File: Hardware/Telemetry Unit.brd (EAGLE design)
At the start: 160 x 100 mm, 12 parts, among them IC1 MEGA128-A, Q1 10MHz, U1 MPL3115A2, X1 SMA-142-0701-801/806

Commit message: First Pass at Compact Layout
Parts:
- removed X1: SMA-142-0701-801/806, con-coax:J502-ND-142-0701-801/806
- added B1: 9V_CLIP, TrackerPeripherals:9V_CLIP
- added C10, C9: 22u, resistor:C0805
- added C11, C7, C8: 22p, resistor:C0603
- added C5, C6: 2.2u, resistor:C0603
- added D1: (no value), diode:DO214AC
- added FIX, PWR: (no value), led:SML0603
- added L1: 1.8n, TrackerPeripherals:L0603
- added L2: 6.8u, TrackerPeripherals:L1210
- added R1, R6: 10k, resistor:R0603
- added R10: 100k, resistor:R0603
- added R11, R2: 470, resistor:R0603
- added R3: 30k, resistor:R0603
- added R7: 40.2k, resistor:R0603
- added R8: 59k, resistor:R0603
- added R9: 13k, resistor:R0603
- added S1: TACT_SW_4.5MM, TrackerPeripherals:TACT_SW_4.5MM
- added U2: AP65111A, TrackerPeripherals:TSOT23-6
- C1: value (none) -> 2.2u
- GPS1: value TESO-LIV3F -> M20048-1; device ITCPeripherals:TESEO-LIV3F -> TrackerPeripherals:M20048-1
- Q1: device crystal:CTS406 -> crystal:HC49UP
- U1: device ITCPeripherals:LGA8 -> TrackerPeripherals:LGA8
- moved C2 41.3 mm to (4.19, 32.4), turned to 180 degrees
- moved C1 35.4 mm to (4.19, 29.8), turned to 180 degrees
- moved C3 31.1 mm to (27.9, 32.4), turned to 180 degrees
- moved C4 30.3 mm to (20.3, 32.4)
- moved XB1 28.3 mm to (34.3, 47.6), turned to 0 degrees
- moved R4 26.6 mm to (13.6, 28.7), turned to 180 degrees
- moved R5 22.2 mm to (13.6, 26.5), turned to 180 degrees
- moved U1 22.2 mm to (7.62, 31.8)
- moved Q1 21.7 mm to (24.1, 27.9)
- moved GPS1 19.2 mm to (11.4, 54.6), turned to 0 degrees
- moved IC1 6.35 mm to (12.7, 15.2), turned to 180 degrees
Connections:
- net N$5 renamed XTAL1
- new net !GPS_SLP: GPS1.26, IC1.30
- new net !RST: IC1.20, R1.2, S1.P$3, XB1.17
- new net FIX: GPS1.18, IC1.29, R2.1
- new net N$10: R8.1, U2.6
- new net N$12: C11.1, U2.4
- new net N$14: PWR.A, R11.2
- new net N$3: C7.2, GPS1.6
- new net N$5: IC1.61, R3.2, R6.1
- new net N$6: FIX.A, R2.2
- new net N$7: C11.2, L2.1, U2.3
- new net N$8: R7.2, R8.2, R9.1
- new net N$9: R10.2, U2.5
- new net PROG_PWR: D1.A, XB1.11
- new net RF_SLP: IC1.31, XB1.9
- new net VBAT: B1.V+, C10.1, D1.C, R10.1, R3.1, U2.1
- new net XTAL2: C3.1, IC1.23, Q1.2
- net +3V3: now also C5.1, C6.1, C8.1, C9.1, GPS1.12, L2.2, R1.1, R11.1, R7.1; no longer GPS1.14, GPS1.6, GPS1.7
- net GND: now also B1.V-, C10.2, C5.2, C6.2, C8.2, C9.2, FIX.C, GPS1.15, GPS1.16, GPS1.17, GPS1.19, GPS1.2, GPS1.22, GPS1.23, GPS1.24, GPS1.25, GPS1.27, GPS1.3, GPS1.5, GPS1.7, GPS1.9, L1.2, PWR.C, R6.2, R9.2, S1.P$2, U2.2; no longer GPS1.1, GPS1.10, GPS1.12, X1.G@1, X1.G@2, X1.G@3, X1.G@4
- net N$1: now also C7.1, GPS1.4; no longer GPS1.11, X1.1
- net N$4: now also GPS1.28, L1.1; no longer C3.1, IC1.23, Q1.3
- net RX1: now also GPS1.20; no longer GPS1.2
- net TX1: now also GPS1.21; no longer GPS1.3
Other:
- board size 160 x 100 mm -> 63.5 x 63.5 mm

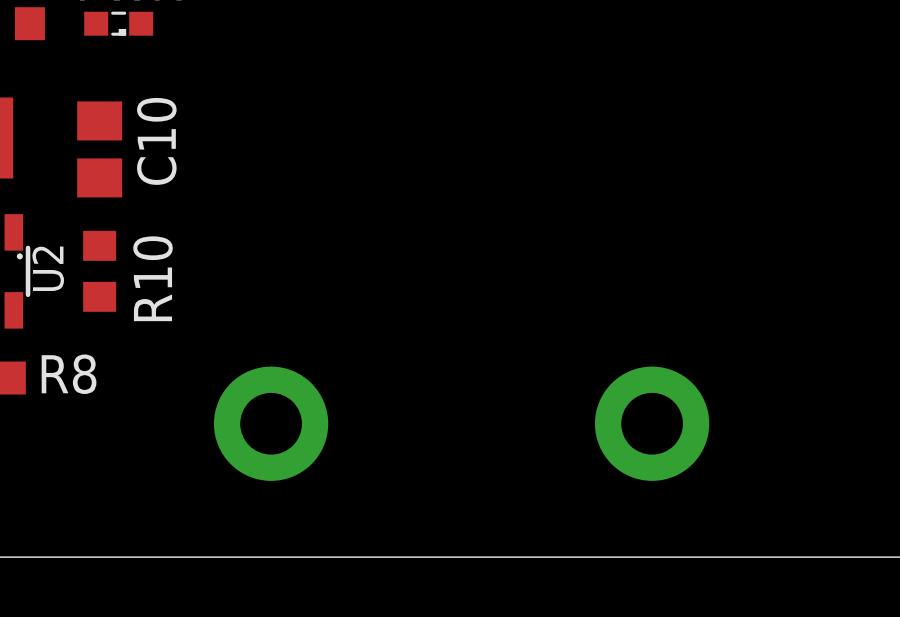
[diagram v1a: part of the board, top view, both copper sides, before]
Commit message: Switch to screw terminals for battery
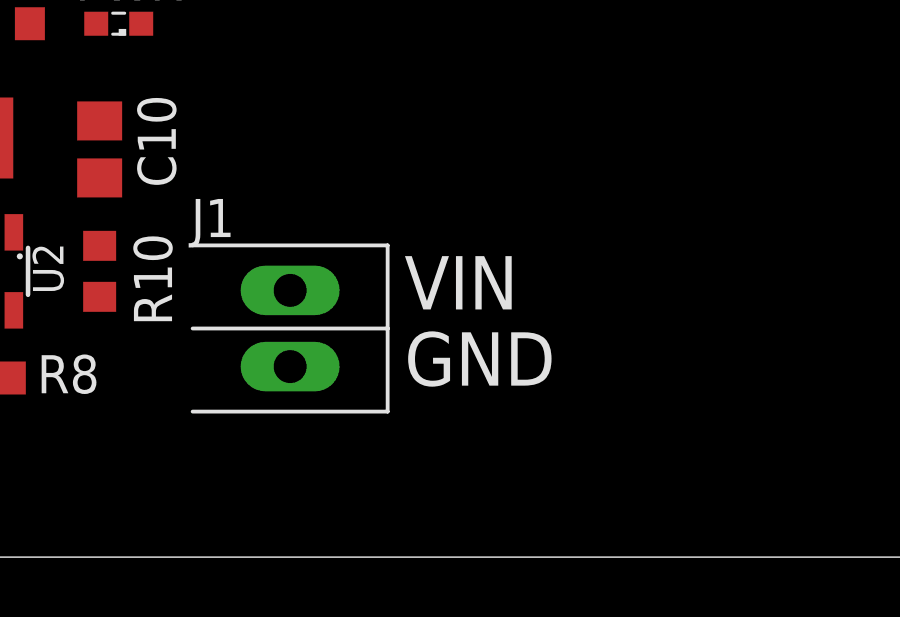
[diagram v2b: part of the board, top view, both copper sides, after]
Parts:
- removed B1: 9V_CLIP, TrackerPeripherals:9V_CLIP
- added J1: (no value), TrackerPeripherals:ST_2X1
- C3, C4: value (none) -> 22p
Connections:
- new net N$11: IC1.20, S1.P$3
- net !RST: now also S1.P$4; no longer IC1.20, S1.P$3
- net GND: now also J1.2; no longer B1.V-
- net VBAT: now also J1.1; no longer B1.V+
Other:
- board text added: "GND"
- board text added: "VIN"
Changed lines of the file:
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@@
 <wire x1="63.5" y1="63.5" x2="0" y2="63.5" width="0" layer="20"/>
 <wire x1="0" y1="63.5" x2="0" y2="0" width="0" layer="20"/>
+<text x="43.815" y="8.255" size="1.778" layer="21">VIN</text>
+<text x="43.815" y="5.715" size="1.778" layer="21">GND</text>
 </plain>
 <attributes>
@@
 </autorouter>
 <elements>
-<element name="C3" library="resistor" library_urn="urn:adsk.eagle:library:348" package="C0603" package3d_urn="urn:adsk.eagle:package:23616/2" value="" x="27.94" y="32.385" smashed="yes" rot="R180">
+<element name="C3" library="resistor" library_urn="urn:adsk.eagle:library:348" package="C0603" package3d_urn="urn:adsk.eagle:package:23616/2" value="22p" x="27.94" y="32.385" smashed="yes" rot="R180">
 <attribute name="NAME" x="28.575" y="34.29" size="1.27" layer="25" rot="R180"/>
 <attribute name="VALUE" x="28.575" y="34.29" size="1.27" layer="27" rot="R180"/>
 </element>
-<element name="C4" library="resistor" library_urn="urn:adsk.eagle:library:348" package="C0603" package3d_urn="urn:adsk.eagle:package:23616/2" value="" x="20.32" y="32.385" smashed="yes">
+<element name="C4" library="resistor" library_urn="urn:adsk.eagle:library:348" package="C0603" package3d_urn="urn:adsk.eagle:package:23616/2" value="22p" x="20.32" y="32.385" smashed="yes">
 <attribute name="NAME" x="19.685" y="33.02" size="1.27" layer="25"/>
 <attribute name="VALUE" x="19.685" y="30.48" size="1.27" layer="27"/>
@@
 <attribute name="VALUE" x="29.845" y="15.875" size="1.27" layer="27"/>
 </element>
-<element name="B1" library="TrackerPeripherals" package="9V_CLIP" value="9V_CLIP" x="45.72" y="4.445" smashed="yes" rot="R270"/>
 <element name="D1" library="diode" library_urn="urn:adsk.eagle:library:210" package="DO214AC" package3d_urn="urn:adsk.eagle:package:43417/2" value="" x="35.56" y="27.305" smashed="yes" rot="R90">
 <attribute name="NAME" x="34.274" y="24.665" size="1.27" layer="25" ratio="10" rot="R90"/>
@@
 <element name="U1" library="TrackerPeripherals" package="LGA8" value="MPL3115A2" x="7.62" y="31.75" smashed="yes">
 <attribute name="NAME" x="6.12" y="34.75" size="1.27" layer="21"/>
+</element>
+<element name="J1" library="TrackerPeripherals" package="ST_2X1" value="" x="40.005" y="7.62" smashed="yes">
+<attribute name="NAME" x="36.703" y="10.668" size="1.27" layer="21"/>
 </element>
 </elements>
@@
 <contactref element="C10" pad="2"/>
 <contactref element="PWR" pad="C"/>
-<contactref element="B1" pad="V-"/>
 <contactref element="U1" pad="3"/>
-<wire x1="18.415" y1="53.225" x2="23.29" y2="38.625" width="0" layer="19" extent="1-1"/>
-<wire x1="15.75" y1="50.21" x2="18.415" y2="53.225" width="0" layer="19" extent="1-1"/>
-<wire x1="15.75" y1="53.51" x2="15.75" y2="50.21" width="0" layer="19" extent="1-1"/>
-<wire x1="15.75" y1="54.61" x2="15.75" y2="53.51" width="0" layer="19" extent="1-1"/>
-<wire x1="15.75" y1="55.71" x2="15.75" y2="54.61" width="0" layer="19" extent="1-1"/>
-<wire x1="15.75" y1="56.81" x2="15.75" y2="55.71" width="0" layer="19" extent="1-1"/>
-<wire x1="15.75" y1="59.01" x2="15.75" y2="56.81" width="0" layer="19" extent="1-1"/>
+<contactref element="J1" pad="2"/>
+<wire x1="15.75" y1="59.01" x2="19.773" y2="60.071" width="0" layer="19" extent="1-1"/>
+<wire x1="15.75" y1="56.81" x2="15.75" y2="59.01" width="0" layer="19" extent="1-1"/>
+<wire x1="15.75" y1="55.71" x2="15.75" y2="56.81" width="0" layer="19" extent="1-1"/>
+<wire x1="15.75" y1="54.61" x2="15.75" y2="55.71" width="0" layer="19" extent="1-1"/>
+<wire x1="15.75" y1="53.51" x2="15.75" y2="54.61" width="0" layer="19" extent="1-1"/>
+<wire x1="18.415" y1="53.225" x2="15.75" y2="53.51" width="0" layer="19" extent="1-1"/>
+<wire x1="15.75" y1="50.21" x2="15.75" y2="53.51" width="0" layer="19" extent="1-1"/>
 <wire x1="14.18" y1="47.31" x2="15.75" y2="50.21" width="0" layer="19" extent="1-1"/>
 <wire x1="13.08" y1="47.31" x2="14.18" y2="47.31" width="0" layer="19" extent="1-1"/>
 <wire x1="11.98" y1="47.31" x2="13.08" y2="47.31" width="0" layer="19" extent="1-1"/>
-<wire x1="19.773" y1="60.071" x2="15.75" y2="59.01" width="0" layer="19" extent="1-1"/>
 <wire x1="7.11" y1="51.31" x2="11.98" y2="47.31" width="0" layer="19" extent="1-1"/>
 <wire x1="7.11" y1="53.51" x2="7.11" y2="51.31" width="0" layer="19" extent="1-1"/>
@@
 <wire x1="7.11" y1="57.91" x2="7.11" y2="55.71" width="0" layer="19" extent="1-1"/>
 <wire x1="7.11" y1="59.01" x2="7.11" y2="57.91" width="0" layer="19" extent="1-1"/>
-<wire x1="4.445" y1="50.585" x2="7.11" y2="53.51" width="0" layer="19" extent="1-1"/>
+<wire x1="4.445" y1="50.585" x2="7.11" y2="51.31" width="0" layer="19" extent="1-1"/>
 <wire x1="1.905" y1="50.585" x2="4.445" y2="50.585" width="0" layer="19" extent="1-1"/>
-<wire x1="6.62" y1="31.125" x2="11.98" y2="47.31" width="0" layer="19" extent="1-1"/>
+<wire x1="23.29" y1="38.625" x2="14.18" y2="47.31" width="0" layer="19" extent="1-1"/>
+<wire x1="21.17" y1="32.385" x2="23.29" y2="38.625" width="0" layer="19" extent="1-1"/>
+<wire x1="27.09" y1="32.385" x2="21.17" y2="32.385" width="0" layer="19" extent="1-1"/>
+<wire x1="14.7" y1="23.04" x2="21.17" y2="32.385" width="0" layer="19" extent="1-1"/>
+<wire x1="6.62" y1="31.125" x2="14.7" y2="23.04" width="0" layer="19" extent="1-1"/>
 <wire x1="3.341" y1="32.385" x2="6.62" y2="31.125" width="0" layer="19" extent="1-1"/>
 <wire x1="3.341" y1="29.845" x2="3.341" y2="32.385" width="0" layer="19" extent="1-1"/>
-<wire x1="21.17" y1="32.385" x2="3.341" y2="29.845" width="0" layer="19" extent="1-1"/>
-<wire x1="14.7" y1="23.04" x2="21.17" y2="32.385" width="0" layer="19" extent="1-1"/>
 <wire x1="27" y1="17.695" x2="14.7" y2="23.04" width="0" layer="19" extent="1-1"/>
 <wire x1="24.257" y1="12.512" x2="27" y2="17.695" width="0" layer="19" extent="1-1"/>
 <wire x1="29.845" y1="10.825" x2="24.257" y2="12.512" width="0" layer="19" extent="1-1"/>
 <wire x1="33.655" y1="14.539" x2="29.845" y2="10.825" width="0" layer="19" extent="1-1"/>
+<wire x1="35.04" y1="17.78" x2="33.655" y2="14.539" width="0" layer="19" extent="1-1"/>
 <wire x1="23.915" y1="5.969" x2="24.257" y2="12.512" width="0" layer="19" extent="1-1"/>
 <wire x1="17.9" y1="7.44" x2="23.915" y2="5.969" width="0" layer="19" extent="1-1"/>
@@
 <wire x1="9.9" y1="7.44" x2="16.93" y2="5.08" width="0" layer="19" extent="1-1"/>
 <wire x1="9.31" y1="5.08" x2="9.9" y2="7.44" width="0" layer="19" extent="1-1"/>
-<wire x1="27.09" y1="32.385" x2="27" y2="17.695" width="0" layer="19" extent="1-1"/>
-<wire x1="52.07" y1="4.445" x2="33.655" y2="14.539" width="0" layer="19" extent="1-1"/>
-<wire x1="35.04" y1="17.78" x2="27.09" y2="32.385" width="0" layer="19" extent="1-1"/>
+<wire x1="40.005" y1="6.35" x2="9.31" y2="5.08" width="0" layer="19" extent="1-1"/>
 </signal>
 <signal name="SDA">
@@
 <signal name="!RST">
 <contactref element="XB1" pad="17"/>
-<contactref element="IC1" pad="20"/>
 <contactref element="R1" pad="2"/>
-<contactref element="S1" pad="P$3"/>
 <wire x1="29.63" y1="22.86" x2="45.29" y2="50.625" width="0" layer="19" extent="1-1"/>
-<wire x1="23.8" y1="22.945" x2="29.63" y2="22.86" width="0" layer="19" extent="1-1"/>
-<wire x1="16.3" y1="23.04" x2="23.8" y2="22.945" width="0" layer="19" extent="1-1"/>
+<wire x1="27" y1="22.945" x2="29.63" y2="22.86" width="0" layer="19" extent="1-1"/>
+<contactref element="S1" pad="P$4"/>
 </signal>
 <signal name="N$1">
@@
 <contactref element="R10" pad="1"/>
 <contactref element="C10" pad="1"/>
-<contactref element="B1" pad="V+"/>
 <contactref element="D1" pad="C"/>
-<wire x1="39.37" y1="4.445" x2="35.56" y2="25.255" width="0" layer="19" extent="1-1"/>
-<wire x1="33.655" y1="12.639" x2="39.37" y2="4.445" width="0" layer="19" extent="1-1"/>
+<contactref element="J1" pad="1"/>
+<wire x1="33.655" y1="12.639" x2="35.56" y2="25.255" width="0" layer="19" extent="1-1"/>
 <wire x1="33.655" y1="10.375" x2="33.655" y2="12.639" width="0" layer="19" extent="1-1"/>
 <wire x1="30.795" y1="10.825" x2="33.655" y2="10.375" width="0" layer="19" extent="1-1"/>
 <wire x1="14.82" y1="5.08" x2="30.795" y2="10.825" width="0" layer="19" extent="1-1"/>
+<wire x1="40.005" y1="8.89" x2="14.82" y2="5.08" width="0" layer="19" extent="1-1"/>
 </signal>
 <signal name="N$10">
@@
 <wire x1="45.29" y1="38.625" x2="35.56" y2="29.355" width="0" layer="19" extent="1-1"/>
 </signal>
+<signal name="N$11">
+<contactref element="IC1" pad="20"/>
+<wire x1="16.3" y1="23.04" x2="23.8" y2="22.945" width="0" layer="19" extent="1-1"/>
+<contactref element="S1" pad="P$3"/>
+</signal>
 </signals>

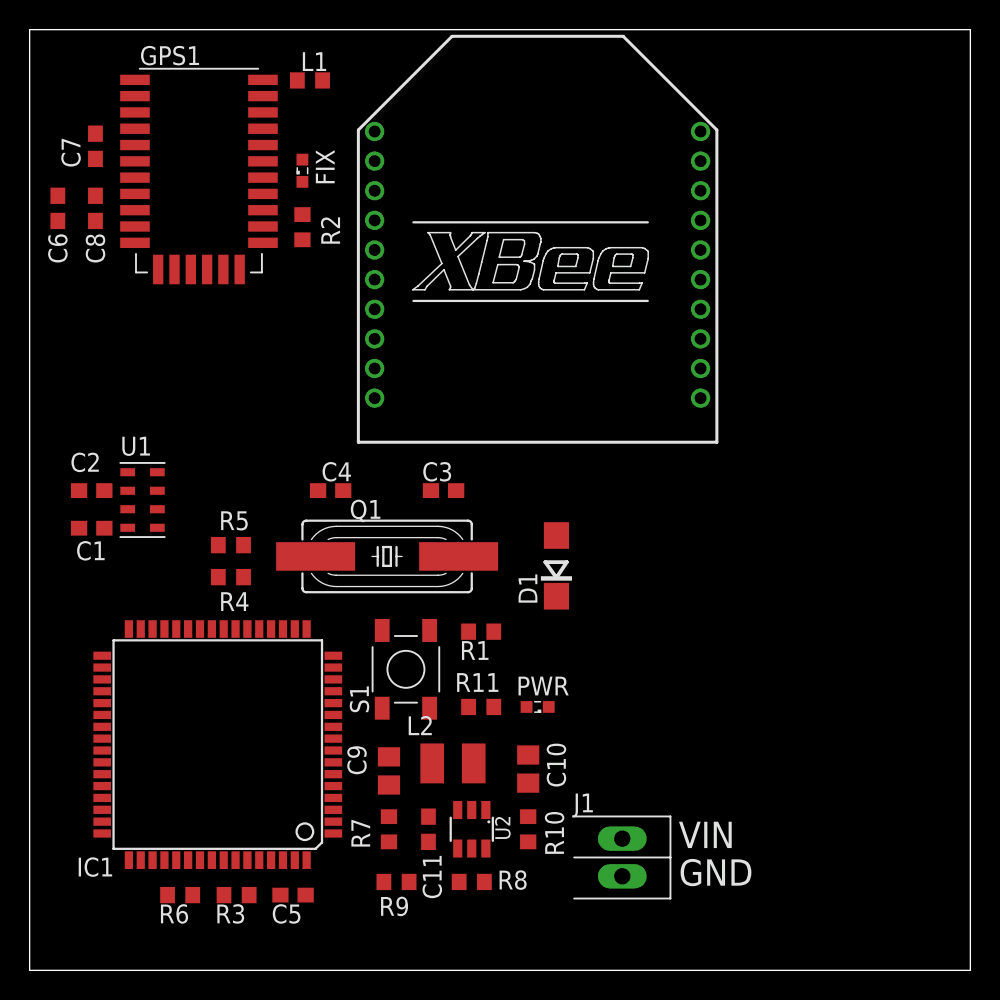
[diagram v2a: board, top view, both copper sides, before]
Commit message: Add accelerometer
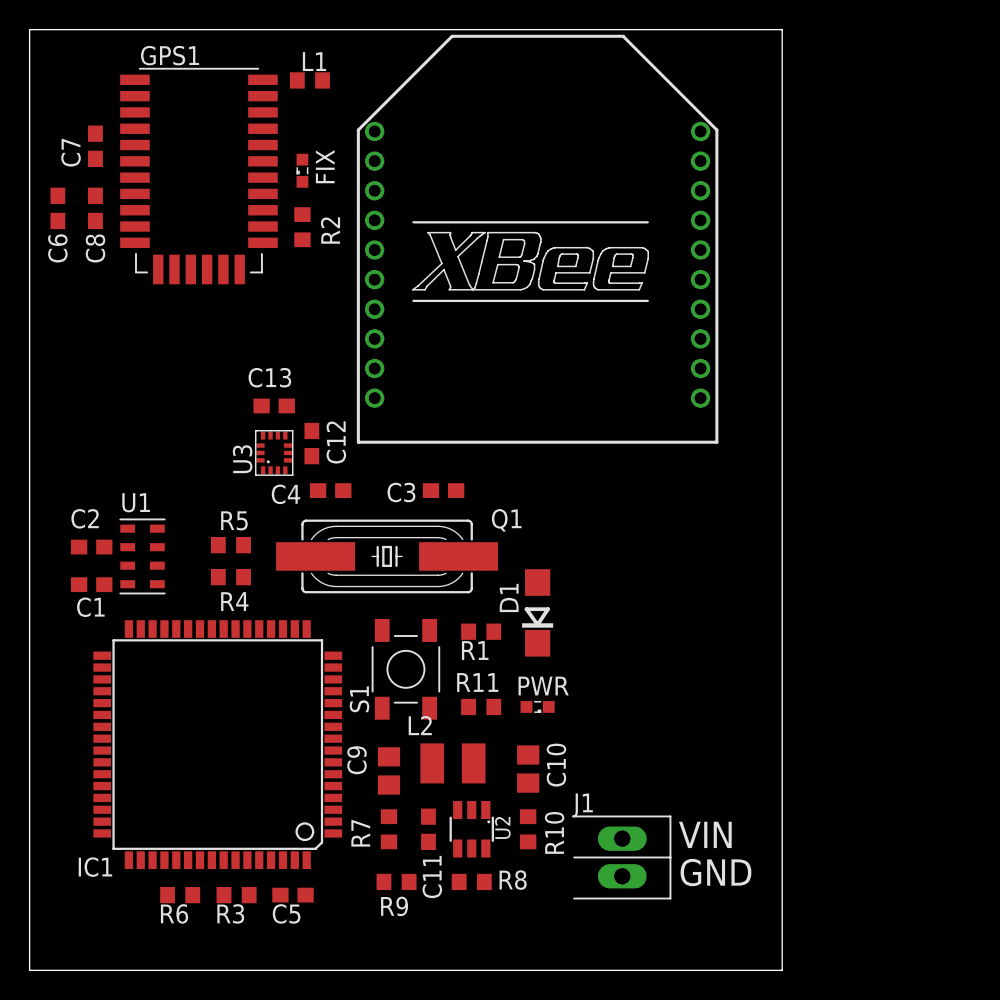
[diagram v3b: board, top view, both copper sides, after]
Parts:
- added C12: 100n, resistor:C0603
- added C13: 2.2u, resistor:C0603
- added U3: LSM6DS3, TrackerPeripherals:14-LGA
- moved C1 3.81 mm to (4.19, 26.0)
- moved C2 3.81 mm to (4.19, 28.6)
- moved U1 3.81 mm to (7.62, 27.9)
- moved D1 3.42 mm to (34.3, 24.1)
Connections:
- new net ACCEL_INT: IC1.6, U3.4
- net +3V3: now also C12.1, C13.1, U3.5, U3.8
- net GND: now also C12.2, C13.2, U3.6, U3.7
- net SCL: now also U3.13
- net SDA: now also U3.14
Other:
- board size 63.5 x 63.5 mm -> 50.8 x 63.5 mm

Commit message: Preliminary Signal Routing
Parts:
- moved C1 0.63 mm to (3.56, 26.0)
- moved C2 0.63 mm to (3.56, 28.6)
- moved FIX 0.63 mm to (18.4, 53.3), turned to 270 degrees
- moved R4 0.25 mm to (13.3, 28.7)
- moved R5 0.25 mm to (13.3, 26.5)
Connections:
- removed net N$11: IC1.20, S1.P$3
- new net RST2: R1.2, S1.P$4
- net !RST: now also IC1.20, S1.P$3; no longer R1.2, S1.P$4
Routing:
- net VBAT: track 0.00 -> 52.4 mm
- net RX0: track 0.00 -> 49.1 mm, vias 0 -> 2
- net TX0: track 0.00 -> 45.0 mm, vias 0 -> 2
- net !GPS_SLP: track 0.00 -> 40.4 mm, vias 0 -> 2
- net FIX: track 0.00 -> 34.5 mm, vias 0 -> 2
- net TX1: track 0.00 -> 32.8 mm, vias 0 -> 2
- net RX1: track 0.00 -> 31.4 mm, vias 0 -> 2
- net RF_SLP: track 0.00 -> 28.1 mm
- net +3V3: track 0.00 -> 27.0 mm
- net ACCEL_INT: track 0.00 -> 22.3 mm, vias 0 -> 2
- net XTAL2: track 0.00 -> 22.2 mm
- net SCL: track 0.00 -> 18.3 mm
- net SDA: track 0.00 -> 17.2 mm, vias 0 -> 2
- net GND: track 0.00 -> 17.1 mm
- net XTAL1: track 0.00 -> 13.2 mm
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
